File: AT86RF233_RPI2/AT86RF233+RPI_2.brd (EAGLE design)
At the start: 23.6 x 43.1 mm, 10 parts, among them U1 ATZB-RF-233-1-C

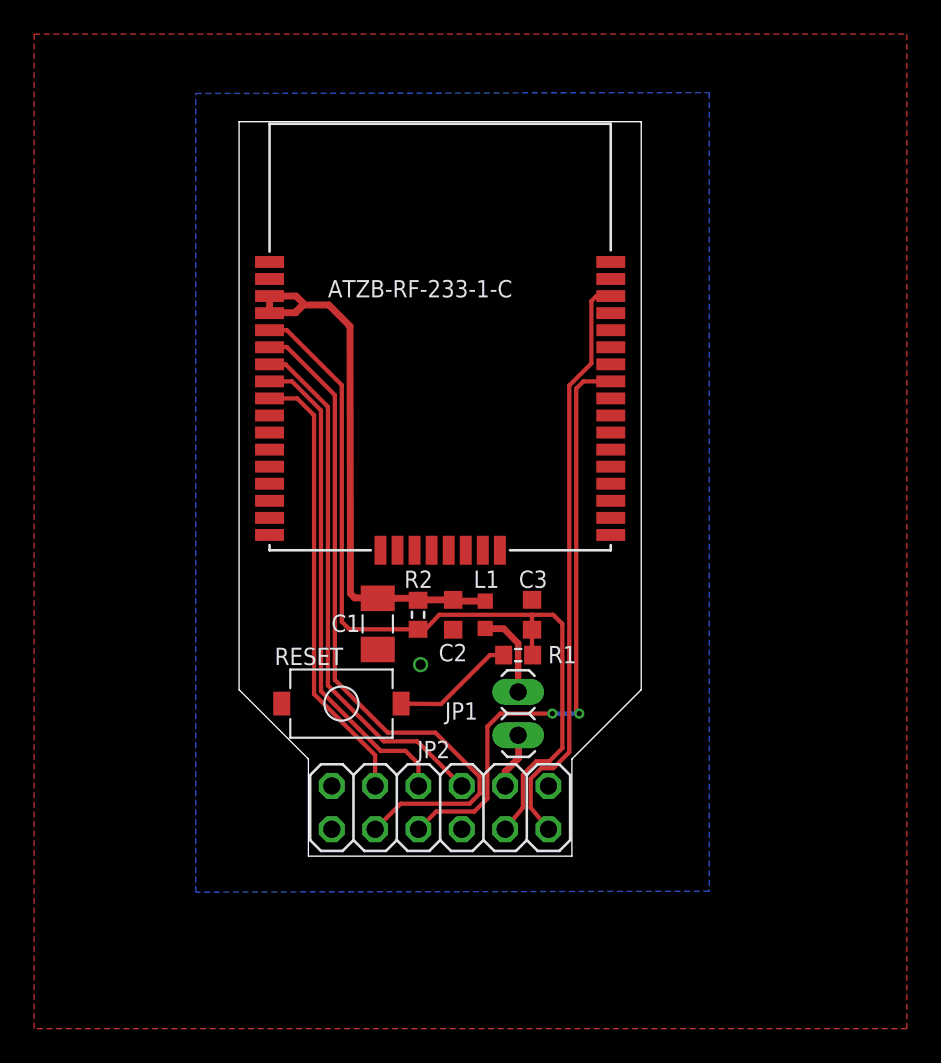
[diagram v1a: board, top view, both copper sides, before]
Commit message: at86rf233: board finalizing
Signed-off-by: malo <malo@25cmsquare.io>
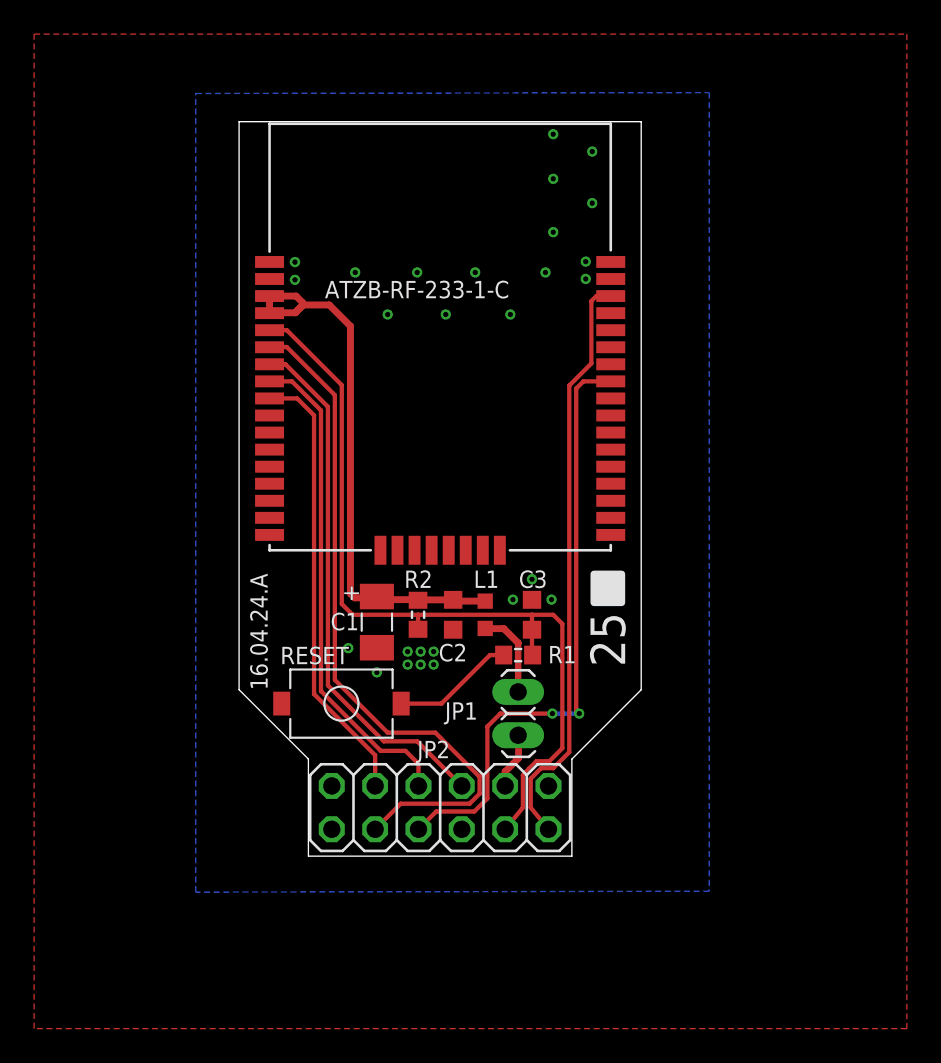
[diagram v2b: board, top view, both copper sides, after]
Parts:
- moved C1 0.11 mm to (8.08, 13.7)
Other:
- board text added: "+"
- board text added: "16.04.24.A"
- board text added: "25"
- board text added: "25cm"
- board text added: "square.io"
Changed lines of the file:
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@@
 <layer number="42" name="bRestrict" color="1" fill="10" visible="yes" active="yes"/>
 <layer number="43" name="vRestrict" color="2" fill="10" visible="yes" active="yes"/>
-<layer number="44" name="Drills" color="7" fill="1" visible="no" active="yes"/>
+<layer number="44" name="Drills" color="7" fill="1" visible="yes" active="yes"/>
 <layer number="45" name="Holes" color="7" fill="1" visible="yes" active="yes"/>
 <layer number="46" name="Milling" color="3" fill="1" visible="yes" active="yes"/>
@@
 <wire x1="0" y1="9.7536" x2="4.064" y2="5.6896" width="0" layer="20"/>
 <wire x1="4.064" y1="5.6896" x2="4.064" y2="0" width="0" layer="20"/>
+<text x="22.6314" y="11.0998" size="2.032" layer="25" font="vector" ratio="15" rot="R90">25</text>
+<polygon width="0.4064" layer="25">
+<vertex x="22.4282" y="14.859"/>
+<vertex x="20.8026" y="14.859"/>
+<vertex x="20.8026" y="16.5354"/>
+<vertex x="22.4282" y="16.5354"/>
+</polygon>
+<text x="14.2174" y="17.7736" size="5.842" layer="26" font="vector" ratio="20" rot="MR270" align="bottom-center">25cm</text>
+<text x="12.9606" y="34.3218" size="1.9304" layer="26" font="vector" ratio="20" rot="MR90" align="bottom-center">square.io</text>
+<text x="1.6764" y="9.7282" size="1.016" layer="25" font="vector" ratio="15" rot="R90">16.04.24.A</text>
+<text x="7.0358" y="14.8844" size="1.016" layer="25" font="vector" ratio="15" rot="R90">+</text>
 </plain>
 <attributes>
@@
 </autorouter>
 <elements>
-<element name="C1" library="resistor" package="C1206K" value="TANTAL 10u 16V 1206, TR3A106K016C" x="8.128" y="13.6144" smashed="yes" rot="R270">
-<attribute name="SPICEPREFIX" value="C" x="8.128" y="13.6144" size="1.778" layer="27" rot="R270" display="off"/>
-<attribute name="NAME" x="5.410396875" y="13.1396" size="1.016" layer="25" font="vector" ratio="15"/>
+<element name="C1" library="resistor" package="C1206K" value="TANTAL 10u 16V 1206, TR3A106K016C" x="8.0772" y="13.716" smashed="yes" rot="R270">
+<attribute name="SPICEPREFIX" value="C" x="8.0772" y="13.716" size="1.778" layer="27" rot="R270" display="off"/>
+<attribute name="NAME" x="5.359596875" y="13.2412" size="1.016" layer="25" font="vector" ratio="15"/>
 </element>
 <element name="C2" library="rcl" package="C0603K" value="1nF, 0603, GRM155R71H1 02K" x="12.5476" y="14.1478" smashed="yes" rot="R270">
@@
 </element>
 <element name="RESET" library="25cmsquare" package="KSR2XYG" value="KSR2XYG" x="9.4996" y="8.9408" smashed="yes" rot="R90">
-<attribute name="NAME" x="2.0828" y="11.2014" size="1.016" layer="21" font="vector" ratio="15"/>
+<attribute name="NAME" x="2.413" y="11.2522" size="1.016" layer="21" font="vector" ratio="15"/>
 </element>
 <element name="U1" library="25cmsquare" package="ATZB-RF-233-1-C" value="ATZB-RF-233-1-C" x="11.7856" y="30.4292" smashed="yes" rot="R180">
-<attribute name="VALUE" x="5.2032" y="32.752" size="1.016" layer="21" font="vector" ratio="15"/>
+<attribute name="VALUE" x="5.0254" y="32.7012" size="1.016" layer="21" font="vector" ratio="15"/>
 </element>
 </elements>
@@
 <vertex x="-12.0142" y="-10.1092"/>
 </polygon>
-<via x="10.6426" y="11.2268" extent="1-16" drill="0.6" shape="square"/>
+<via x="10.6426" y="11.2268" extent="1-16" drill="0.3048"/>
+<via x="11.4046" y="11.2268" extent="1-16" drill="0.3048"/>
+<via x="10.6426" y="11.9888" extent="1-16" drill="0.3048"/>
+<via x="11.4046" y="11.9888" extent="1-16" drill="0.3048"/>
+<via x="16.0528" y="15.0368" extent="1-16" drill="0.3048"/>
+<via x="18.3134" y="15.0368" extent="1-16" drill="0.3048"/>
+<via x="17.1704" y="16.2306" extent="1-16" drill="0.3048"/>
+<via x="9.8806" y="11.2268" extent="1-16" drill="0.3048"/>
+<via x="9.8806" y="11.9888" extent="1-16" drill="0.3048"/>
+<via x="3.2766" y="34.8234" extent="1-16" drill="0.3048"/>
+<via x="3.2766" y="33.782" extent="1-16" drill="0.3048"/>
+<via x="20.32" y="34.8488" extent="1-16" drill="0.3048"/>
+<via x="20.32" y="33.8328" extent="1-16" drill="0.3048"/>
+<via x="8.0772" y="10.7696" extent="1-16" drill="0.3048"/>
+<via x="6.8072" y="34.2138" extent="1-16" drill="0.3048"/>
+<via x="10.4394" y="34.2138" extent="1-16" drill="0.3048"/>
+<via x="13.843" y="34.2138" extent="1-16" drill="0.3048"/>
+<via x="17.9578" y="34.2138" extent="1-16" drill="0.3048"/>
+<via x="18.415" y="39.7002" extent="1-16" drill="0.3048"/>
+<via x="18.415" y="42.3164" extent="1-16" drill="0.3048"/>
+<via x="18.415" y="36.576" extent="1-16" drill="0.3048"/>
+<via x="8.7122" y="31.75" extent="1-16" drill="0.3048"/>
+<via x="12.1158" y="31.75" extent="1-16" drill="0.3048"/>
+<via x="15.9004" y="31.75" extent="1-16" drill="0.3048"/>
+<via x="20.701" y="38.2778" extent="1-16" drill="0.3048"/>
+<via x="20.701" y="41.3004" extent="1-16" drill="0.3048"/>
+<via x="6.4008" y="12.192" extent="1-16" drill="0.3048"/>
 </signal>
 <signal name="VCC_ATZB_3V3">
@@
 <wire x1="1.7856" y1="31.8292" x2="1.7856" y2="32.8292" width="0.4064" layer="1"/>
 <wire x1="1.7856" y1="31.8292" x2="1.7886" y2="31.8262" width="0.4064" layer="1"/>
-<wire x1="6.5024" y1="31.0642" x2="6.5278" y2="15.3924" width="0.4064" layer="1"/>
+<wire x1="6.5278" y1="31.0642" x2="6.5278" y2="15.3924" width="0.4064" layer="1"/>
 <wire x1="6.5278" y1="15.3924" x2="6.7818" y2="15.1384" width="0.4064" layer="1"/>
 <contactref element="L1" pad="2"/>
@@
 <wire x1="3.302" y1="31.8516" x2="3.302" y2="31.877" width="0.4064" layer="1"/>
 <wire x1="3.302" y1="31.877" x2="3.7338" y2="32.3088" width="0.4064" layer="1"/>
-<wire x1="3.7338" y1="32.3088" x2="5.2578" y2="32.3088" width="0.4064" layer="1"/>
-<wire x1="5.2578" y1="32.3088" x2="6.5024" y2="31.0642" width="0.4064" layer="1"/>
+<wire x1="3.7338" y1="32.3088" x2="5.2832" y2="32.3088" width="0.4064" layer="1"/>
 <wire x1="6.7818" y1="15.1384" x2="8.104" y2="15.1384" width="0.4064" layer="1"/>
-<wire x1="8.104" y1="15.1384" x2="8.128" y2="15.1144" width="0.4064" layer="1"/>
-<wire x1="8.128" y1="15.1144" x2="10.3736" y2="15.1144" width="0.4064" layer="1"/>
+<wire x1="8.104" y1="15.1384" x2="8.0772" y2="15.216" width="0.4064" layer="1"/>
 <wire x1="10.3736" y1="15.1144" x2="10.4902" y2="14.9978" width="0.4064" layer="1"/>
 <wire x1="10.4902" y1="14.9978" x2="10.5152" y2="15.0228" width="0.4064" layer="1"/>
@@
 <wire x1="12.5476" y1="15.0228" x2="12.6226" y2="14.9478" width="0.4064" layer="1"/>
 <wire x1="12.6226" y1="14.9478" x2="14.4272" y2="14.9478" width="0.4064" layer="1"/>
+<wire x1="10.3736" y1="15.1144" x2="10.296" y2="15.0368" width="0.4064" layer="1"/>
+<wire x1="10.296" y1="15.0368" x2="8.89" y2="15.0368" width="0.4064" layer="1"/>
+<wire x1="8.89" y1="15.0368" x2="8.7108" y2="15.216" width="0.4064" layer="1"/>
+<wire x1="8.7108" y1="15.216" x2="8.0772" y2="15.216" width="0.4064" layer="1"/>
+<wire x1="5.2832" y1="32.3088" x2="6.5278" y2="31.0642" width="0.4064" layer="1"/>
 </signal>
 <signal name="MOSI">
@@
 <wire x1="15.5956" y1="1.5748" x2="16.637" y2="2.8448" width="0.254" layer="1"/>
 <wire x1="16.637" y1="2.8448" x2="16.637" y2="4.7498" width="0.254" layer="1"/>
-<wire x1="6.0198" y1="27.6098" x2="6.0198" y2="13.7414" width="0.254" layer="1"/>
+<wire x1="6.0198" y1="27.6098" x2="6.0198" y2="14.7828" width="0.254" layer="1"/>
 <wire x1="2.8004" y1="30.8292" x2="6.0198" y2="27.6098" width="0.254" layer="1"/>
 <wire x1="10.4902" y1="13.2978" x2="10.5406" y2="13.1458" width="0.254" layer="1"/>
-<wire x1="6.0198" y1="13.7414" x2="6.4634" y2="13.2978" width="0.254" layer="1"/>
-<wire x1="6.4634" y1="13.2978" x2="10.4902" y2="13.2978" width="0.254" layer="1"/>
 <wire x1="16.637" y1="4.7498" x2="17.018" y2="5.1562" width="0.254" layer="1"/>
 <wire x1="18.9484" y1="6.3246" x2="18.9484" y2="13.6144" width="0.254" layer="1"/>
@@
 <wire x1="17.4244" y1="5.5626" x2="18.1864" y2="5.5626" width="0.254" layer="1"/>
 <wire x1="18.415" y1="14.1478" x2="17.1704" y2="14.1478" width="0.254" layer="1"/>
-<wire x1="17.1704" y1="14.1478" x2="11.7348" y2="14.1478" width="0.254" layer="1"/>
-<wire x1="11.7348" y1="14.1478" x2="10.7442" y2="13.1064" width="0.254" layer="1"/>
+<wire x1="17.1704" y1="14.1478" x2="10.4902" y2="14.1478" width="0.254" layer="1"/>
+<wire x1="10.4902" y1="14.1478" x2="6.6548" y2="14.1478" width="0.254" layer="1"/>
 <wire x1="10.7442" y1="13.1064" x2="10.5038" y2="13.1572" width="0.254" layer="1"/>
 <wire x1="10.5038" y1="13.1572" x2="10.4902" y2="13.2978" width="0.254" layer="1"/>
@@
 <wire x1="17.2076" y1="11.7856" x2="17.1704" y2="11.7856" width="0.254" layer="1"/>
 <wire x1="17.1704" y1="11.7856" x2="17.1704" y2="13.2728" width="0.254" layer="1"/>
+<wire x1="10.4902" y1="13.2978" x2="10.4902" y2="14.1478" width="0.254" layer="1"/>
+<wire x1="6.0198" y1="14.7828" x2="6.6548" y2="14.1478" width="0.254" layer="1"/>
 </signal>
 <signal name="SLP_TR">
@@
 <contactref element="R1" pad="1"/>
 <contactref element="RESET" pad="P$1"/>
-<wire x1="9.4996" y1="8.9408" x2="11.8364" y2="8.9154" width="0.254" layer="1"/>
-<wire x1="11.8364" y1="8.9154" x2="14.7066" y2="11.7856" width="0.254" layer="1"/>
+<wire x1="9.4996" y1="8.9408" x2="11.8618" y2="8.9408" width="0.254" layer="1"/>
+<wire x1="11.8618" y1="8.9408" x2="14.7066" y2="11.7856" width="0.254" layer="1"/>
 <wire x1="15.5076" y1="11.7856" x2="14.7066" y2="11.7856" width="0.254" layer="1"/>
 </signal>
@@
 <contactref element="L1" pad="1"/>
 <wire x1="16.3576" y1="9.6266" x2="16.3576" y2="12.4714" width="0.381" layer="1"/>
-<wire x1="16.3576" y1="12.4714" x2="15.5194" y2="13.335" width="0.381" layer="1"/>
 <wire x1="15.5194" y1="13.335" x2="14.44" y2="13.335" width="0.4064" layer="1"/>
 <wire x1="14.44" y1="13.335" x2="14.4272" y2="13.3478" width="0.4064" layer="1"/>
+<wire x1="16.3576" y1="12.4714" x2="16.3576" y2="12.4968" width="0.4064" layer="1"/>
+<wire x1="16.3576" y1="12.4968" x2="15.5194" y2="13.335" width="0.4064" layer="1"/>
 </signal>
 </signals>
